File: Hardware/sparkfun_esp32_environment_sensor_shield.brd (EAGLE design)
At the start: 58.4 x 50.8 mm, 49 parts, among them J1 WEATHER_METER-WIND, J2 WEATHER_METER-RAIN, U1 BME280, U2 CCS811, U3 TSL2561FN, U4 TVS Diode

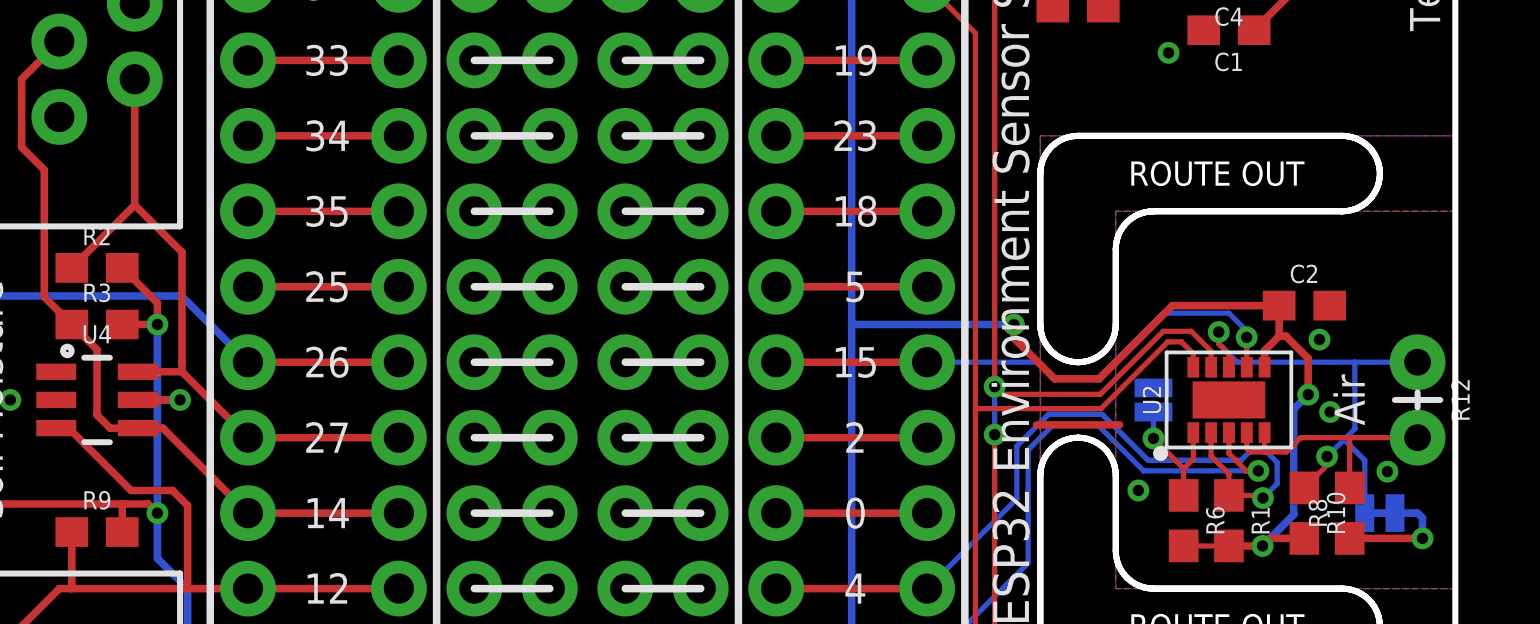
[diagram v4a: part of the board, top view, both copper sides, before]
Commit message: Adjustin silkscreen, adding measures to RJ11 jacks, screw terminals.
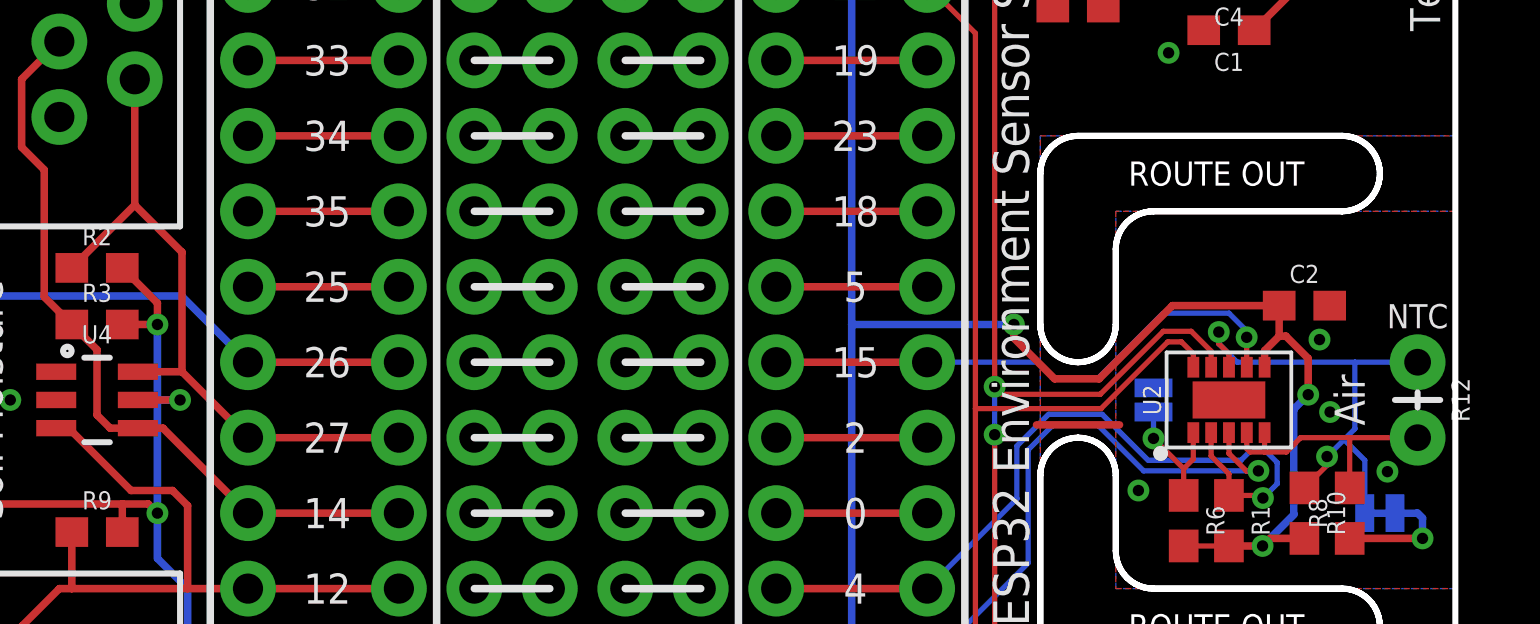
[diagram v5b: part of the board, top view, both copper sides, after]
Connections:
- net INT_TSL2561 renamed TSL2561_INT
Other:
- board text added: "NTC"
- board text added: "Units in inches"
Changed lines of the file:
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@@
 DIR</text>
 <text x="16.51" y="26.67" size="0.889" layer="22" font="vector" ratio="15" rot="MR0" align="center-left">SOIL</text>
-<dimension x1="0" y1="0" x2="0" y2="50.8" x3="-7.62" y3="25.4" textsize="0.889" textratio="15" layer="47" dtype="vertical" unit="inch" precision="3"/>
-<dimension x1="2.54" y1="48.26" x2="2.54" y2="0" x3="-5.08" y3="24.13" textsize="0.889" textratio="15" layer="47" dtype="vertical" unit="inch" precision="3"/>
+<dimension x1="0" y1="0" x2="0" y2="50.8" x3="-15.24" y3="25.4" textsize="0.889" textratio="15" layer="47" dtype="vertical" unit="inch" precision="3"/>
+<dimension x1="2.54" y1="48.26" x2="2.54" y2="0" x3="-12.7" y3="24.13" textsize="0.889" textratio="15" layer="47" dtype="vertical" unit="inch" precision="3"/>
 <dimension x1="2.54" y1="2.54" x2="-2.54" y2="0" x3="-2.54" y3="1.27" textsize="0.889" textratio="15" layer="47" dtype="vertical" unit="inch" precision="3"/>
-<dimension x1="58.42" y1="0" x2="0" y2="0" x3="29.21" y3="-7.62" textsize="0.889" textratio="15" layer="47" dtype="horizontal" unit="inch" precision="3"/>
-<dimension x1="55.88" y1="2.54" x2="0" y2="2.54" x3="27.94" y3="-5.08" textsize="0.889" textratio="15" layer="47" dtype="horizontal" unit="inch" precision="3"/>
+<dimension x1="58.42" y1="0" x2="0" y2="0" x3="29.21" y3="-12.7" textsize="0.889" textratio="15" layer="47" dtype="horizontal" unit="inch" precision="3"/>
+<dimension x1="55.88" y1="2.54" x2="0" y2="2.54" x3="27.94" y3="-10.16" textsize="0.889" textratio="15" layer="47" dtype="horizontal" unit="inch" precision="3"/>
 <dimension x1="2.54" y1="2.54" x2="0" y2="2.54" x3="1.27" y3="-2.54" textsize="0.889" textratio="15" layer="47" dtype="horizontal" unit="inch" precision="3"/>
 <polygon width="0.2032" layer="46">
@@
 <vertex x="44.45" y="22.86" curve="-90"/>
 </polygon>
+<dimension x1="5.08" y1="12.7" x2="5.08" y2="0" x3="-5.08" y3="6.35" textsize="0.889" textratio="15" layer="47" dtype="vertical" unit="inch" precision="3"/>
+<dimension x1="1.27" y1="22.86" x2="1.27" y2="0" x3="-7.62" y3="11.43" textsize="0.889" textratio="15" layer="47" dtype="vertical" unit="inch" precision="3"/>
+<dimension x1="5.08" y1="12.7" x2="0" y2="11.43" x3="2.54" y3="-7.62" textsize="0.889" textratio="15" layer="47" dtype="horizontal" unit="inch" precision="3"/>
+<dimension x1="3.556" y1="28.9" x2="0" y2="27.94" x3="1.778" y3="-5.08" textsize="0.889" textratio="15" layer="47" dtype="horizontal" unit="inch" precision="3"/>
+<dimension x1="3.556" y1="28.9" x2="5.08" y2="0" x3="-10.16" y3="14.45" textsize="0.889" textratio="15" layer="47" dtype="vertical" unit="inch" precision="3"/>
+<text x="-12.7" y="-10.16" size="0.889" layer="47" ratio="15">Units in inches</text>
+<text x="57.15" y="27.813" size="0.8128" layer="21" ratio="15" align="bottom-center">NTC</text>
 </plain>
 <attributes>
@@
 <wire x1="52.705" y1="10.16" x2="53.975" y2="10.16" width="0.1778" layer="16"/>
 </signal>
-<signal name="INT_TSL2561">
+<signal name="TSL2561_INT">
 <contactref element="U3" pad="5"/>
 <contactref element="B1" pad="35"/>
@@
 <wire x1="17.78" y1="24.13" x2="15.56" y2="26.35" width="0.254" layer="1"/>
 <contactref element="U4" pad="6"/>
-<wire x1="15.56" y1="26.67" x2="15.56" y2="30.375" width="0.254" layer="1"/>
+<wire x1="15.56" y1="26.35" x2="15.56" y2="30.375" width="0.254" layer="1"/>
 <wire x1="14.0751" y1="26.35" x2="15.56" y2="26.35" width="0.254" layer="1"/>
-<wire x1="15.56" y1="26.35" x2="15.56" y2="26.67" width="0.254" layer="1"/>
 </signal>
 <signal name="WIND_SPEED">

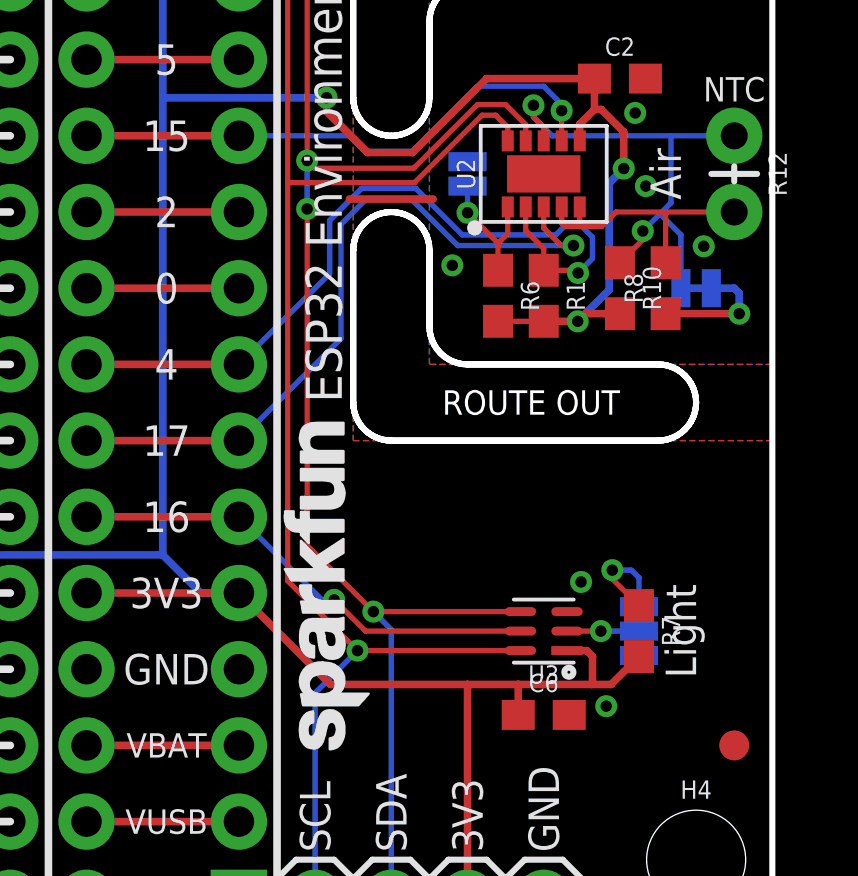
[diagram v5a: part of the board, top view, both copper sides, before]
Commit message: Replaced TLS2561 sensor with APDS-9301
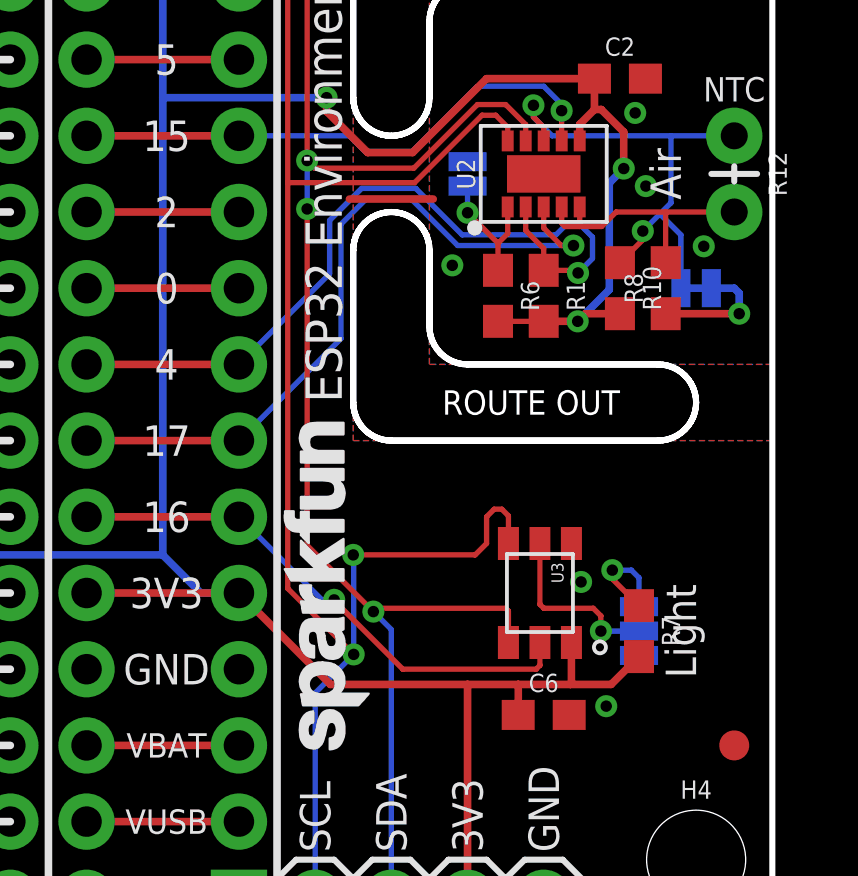
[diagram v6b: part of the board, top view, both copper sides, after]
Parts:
- U3: value TSL2561FN -> APDS-9301; device SparkFun-Sensors:DFN-6-2X2 -> SparkFun-Sensors:CHIPLED-6
- moved U3 1.28 mm to (50.7, 11.4), turned to 270 degrees
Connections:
- removed net TSL2561_INT: B1.35, J13.6, U3.5
- new net LUX_INT: B1.35, J13.6, U3.P6
- net 3.3V: now also U3.P1; no longer U3.1
- net ADDR_TSL2561: now also U3.P3; no longer U3.2
- net GND: now also U3.P2; no longer U3.3
- net SCL: now also U3.P4; no longer U3.6
- net SDA: now also U3.P5; no longer U3.4
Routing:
- net LUX_INT: track 0.00 -> 18.0 mm, vias 0 -> 1
- net TSL2561_INT: track 16.0 -> 0.00 mm, vias 1 -> 0
- net SCL: track 73.5 -> 78.6 mm, vias 3 -> 4
- net ADDR_TSL2561: track 2.40 -> 6.00 mm
- net SDA: track 76.2 -> 76.9 mm

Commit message: Feedback from review
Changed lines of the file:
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@@
 <layer number="20" name="Dimension" color="15" fill="1" visible="yes" active="yes"/>
 <layer number="21" name="tPlace" color="16" fill="1" visible="yes" active="yes"/>
-<layer number="22" name="bPlace" color="14" fill="1" visible="yes" active="yes"/>
+<layer number="22" name="bPlace" color="14" fill="1" visible="no" active="yes"/>
 <layer number="23" name="tOrigins" color="15" fill="1" visible="yes" active="yes"/>
-<layer number="24" name="bOrigins" color="15" fill="1" visible="yes" active="yes"/>
-<layer number="25" name="tNames" color="7" fill="1" visible="no" active="yes"/>
+<layer number="24" name="bOrigins" color="15" fill="1" visible="no" active="yes"/>
+<layer number="25" name="tNames" color="7" fill="1" visible="yes" active="yes"/>
 <layer number="26" name="bNames" color="7" fill="1" visible="no" active="yes"/>
 <layer number="27" name="tValues" color="7" fill="1" visible="no" active="yes"/>
@@
 <layer number="43" name="vRestrict" color="2" fill="10" visible="no" active="yes"/>
 <layer number="44" name="Drills" color="7" fill="1" visible="no" active="yes"/>
-<layer number="45" name="Holes" color="7" fill="1" visible="yes" active="yes"/>
+<layer number="45" name="Holes" color="7" fill="1" visible="no" active="yes"/>
 <layer number="46" name="Milling" color="3" fill="1" visible="no" active="yes"/>
 <layer number="47" name="Measures" color="7" fill="1" visible="no" active="yes"/>
 <layer number="48" name="Document" color="7" fill="1" visible="no" active="yes"/>
 <layer number="49" name="Reference" color="7" fill="1" visible="no" active="yes"/>
-<layer number="51" name="tDocu" color="6" fill="1" visible="yes" active="yes"/>
+<layer number="51" name="tDocu" color="6" fill="1" visible="no" active="yes"/>
 <layer number="52" name="bDocu" color="7" fill="1" visible="no" active="yes"/>
 <layer number="3" name="Route3" color="4" fill="3" visible="no" active="no"/>
@@
 <text x="48.26" y="2.794" size="1.016" layer="21" font="vector" ratio="15" rot="R90" align="center-left">3V3</text>
 <text x="50.8" y="2.794" size="1.016" layer="21" font="vector" ratio="15" rot="R90" align="center-left">GND</text>
-<text x="54.864" y="10.16" size="1.016" layer="21" font="vector" ratio="15" rot="R270" align="bottom-center">Light</text>
+<text x="55.372" y="11.43" size="1.016" layer="21" font="vector" ratio="15" rot="R270" align="bottom-center">Light</text>
 <text x="54.356" y="25.4" size="1.016" layer="21" font="vector" ratio="15" rot="R270" align="bottom-center">Air</text>
 <text x="53.848" y="41.91" size="1.016" layer="21" font="vector" ratio="15" rot="R90" align="top-center">Pressure
@@
 <wire x1="44.87" y1="39.2802" x2="44.3992" y2="39.751" width="0.1778" layer="1"/>
 <contactref element="U3" pad="P4"/>
-<wire x1="44.465" y1="9.383" x2="44.465" y2="12.685" width="0.1778" layer="16"/>
-<wire x1="44.465" y1="12.685" x2="44.45" y2="12.7" width="0.1778" layer="16"/>
-<via x="44.45" y="12.7" extent="1-16" drill="0.381"/>
-<wire x1="44.45" y1="12.7" x2="48.514" y2="12.7" width="0.1778" layer="1"/>
-<wire x1="48.514" y1="12.7" x2="48.895" y2="13.081" width="0.1778" layer="1"/>
-<wire x1="48.895" y1="13.081" x2="48.895" y2="13.97" width="0.1778" layer="1"/>
-<wire x1="48.895" y1="13.97" x2="49.149" y2="14.224" width="0.1778" layer="1"/>
-<wire x1="49.149" y1="14.224" x2="49.403" y2="14.224" width="0.1778" layer="1"/>
+<wire x1="44.465" y1="9.383" x2="44.465" y2="14.082" width="0.1778" layer="16"/>
+<via x="44.45" y="14.097" extent="1-16" drill="0.381"/>
 <wire x1="49.403" y1="14.224" x2="49.623" y2="14.004" width="0.1778" layer="1"/>
 <wire x1="49.623" y1="13.08" x2="49.623" y2="14.004" width="0.1778" layer="1"/>
+<wire x1="49.403" y1="14.224" x2="44.577" y2="14.224" width="0.1778" layer="1"/>
+<wire x1="44.577" y1="14.224" x2="44.45" y2="14.097" width="0.1778" layer="1"/>
+<wire x1="44.465" y1="14.082" x2="44.45" y2="14.097" width="0.1778" layer="16"/>
 </signal>
 <signal name="SDA">

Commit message: Chg rev to 02
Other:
- board text added: "V02"
- board text removed: "V01"
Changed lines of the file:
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@@
 <layer number="20" name="Dimension" color="15" fill="1" visible="yes" active="yes"/>
 <layer number="21" name="tPlace" color="16" fill="1" visible="yes" active="yes"/>
-<layer number="22" name="bPlace" color="14" fill="1" visible="no" active="yes"/>
+<layer number="22" name="bPlace" color="14" fill="1" visible="yes" active="yes"/>
 <layer number="23" name="tOrigins" color="15" fill="1" visible="yes" active="yes"/>
-<layer number="24" name="bOrigins" color="15" fill="1" visible="no" active="yes"/>
-<layer number="25" name="tNames" color="7" fill="1" visible="yes" active="yes"/>
+<layer number="24" name="bOrigins" color="15" fill="1" visible="yes" active="yes"/>
+<layer number="25" name="tNames" color="7" fill="1" visible="no" active="yes"/>
 <layer number="26" name="bNames" color="7" fill="1" visible="no" active="yes"/>
 <layer number="27" name="tValues" color="7" fill="1" visible="no" active="yes"/>
@@
 <layer number="43" name="vRestrict" color="2" fill="10" visible="no" active="yes"/>
 <layer number="44" name="Drills" color="7" fill="1" visible="no" active="yes"/>
-<layer number="45" name="Holes" color="7" fill="1" visible="no" active="yes"/>
+<layer number="45" name="Holes" color="7" fill="1" visible="yes" active="yes"/>
 <layer number="46" name="Milling" color="3" fill="1" visible="no" active="yes"/>
 <layer number="47" name="Measures" color="7" fill="1" visible="no" active="yes"/>
 <layer number="48" name="Document" color="7" fill="1" visible="no" active="yes"/>
 <layer number="49" name="Reference" color="7" fill="1" visible="no" active="yes"/>
-<layer number="51" name="tDocu" color="6" fill="1" visible="no" active="yes"/>
+<layer number="51" name="tDocu" color="6" fill="1" visible="yes" active="yes"/>
 <layer number="52" name="bDocu" color="7" fill="1" visible="no" active="yes"/>
 <layer number="3" name="Route3" color="4" fill="3" visible="no" active="no"/>
@@
 <text x="3.048" y="38.608" size="1.016" layer="22" ratio="15" rot="MR270" align="bottom-center">ESP32 Environment
 Sensor Shield</text>
-<text x="5.207" y="0.254" size="1.016" layer="16" ratio="15" rot="MR0" align="bottom-center">V01</text>
+<text x="5.207" y="0.254" size="1.016" layer="16" ratio="15" rot="MR0" align="bottom-center">V02</text>
 <text x="49.53" y="25.4" size="0.889" layer="22" ratio="15" rot="MR90" align="bottom-center">JP2</text>
 <text x="50.8" y="45.593" size="0.889" layer="22" ratio="15" rot="MR0" align="bottom-center">JP1</text>
